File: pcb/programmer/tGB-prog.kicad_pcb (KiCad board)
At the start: 2 copper layers, 25.2 x 31 mm, 40 parts, among them J1 ZX62R-B-5P, J2 PROG_PORT, U1 FT2232D, U2 93LC56BT-I/OT, U3 TPS79901DDCR, Y1 NX8045GB-6MHZ-STD-CSF-3

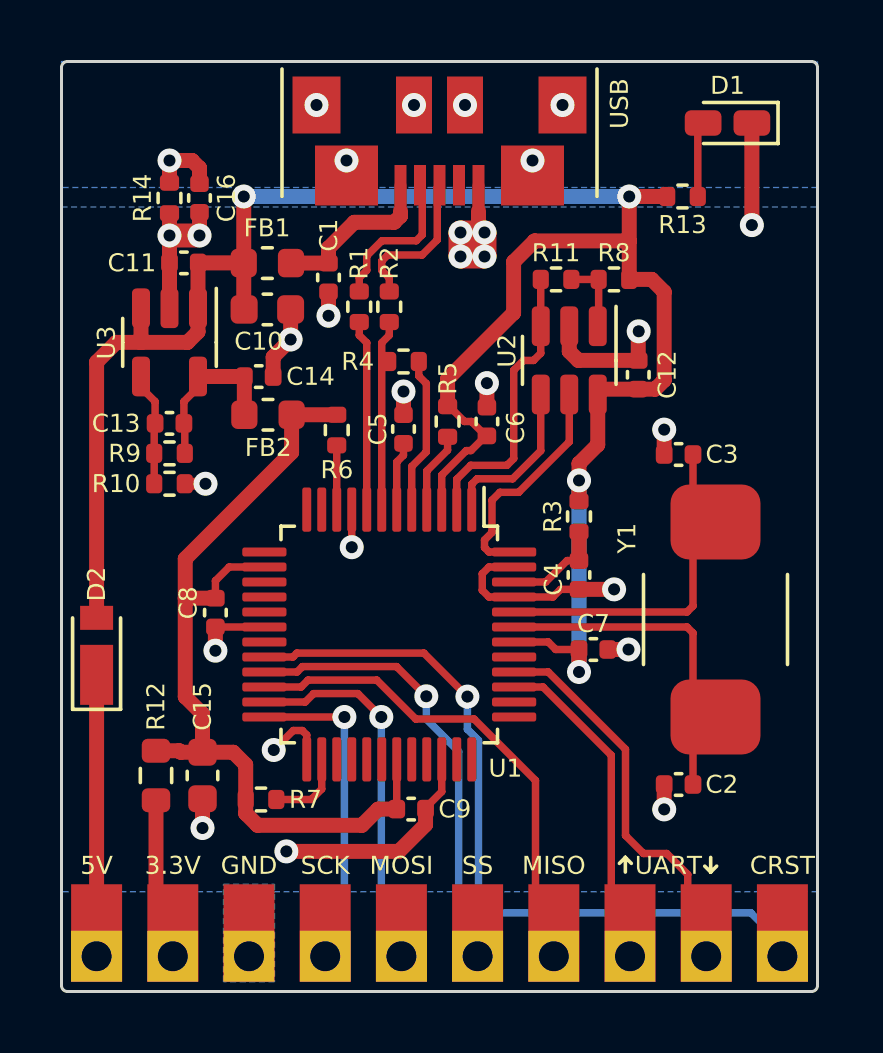
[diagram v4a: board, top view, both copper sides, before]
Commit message: optimize GND and shield zone, fillet USB data tracks
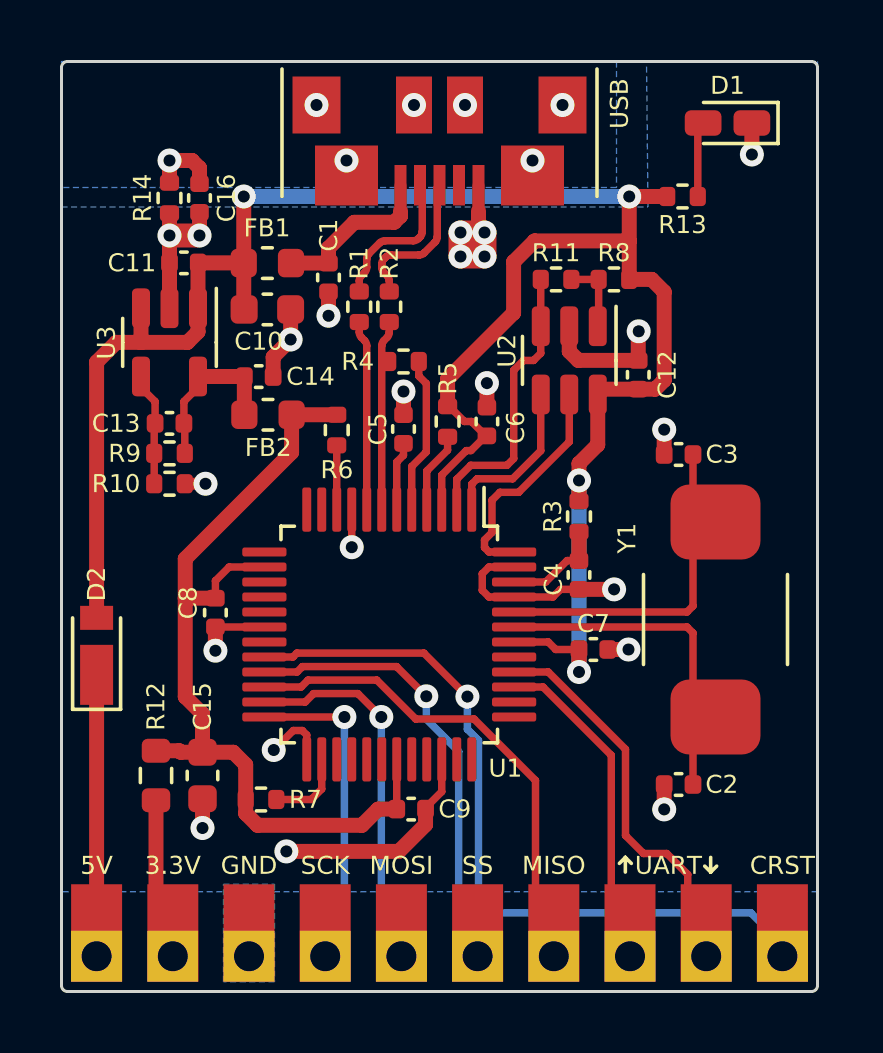
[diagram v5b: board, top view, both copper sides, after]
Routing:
- net GND: track 45.9 -> 43.6 mm
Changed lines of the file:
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@@
   (segment (start 78.9 88.6) (end 78.21 88.6) (width 0.5) (layer "F.Cu") (net 2))
   (segment (start 73.3 74.7) (end 73.3 75.5) (width 0.8) (layer "F.Cu") (net 2))
+  (segment (start 83.0125 71.05) (end 83.0125 72.1) (width 0.5) (layer "F.Cu") (net 2))
   (segment (start 80.09 82.1) (end 80.09 81.27) (width 0.5) (layer "F.Cu") (net 2))
   (segment (start 79.225 78.9625) (end 79.225 78.008052) (width 0.5) (layer "F.Cu") (net 2))
@@
   (segment (start 77.25 86.595) (end 78.42 86.595) (width 0.5) (layer "F.Cu") (net 2))
   (segment (start 67.6375 77.265) (end 67.6375 78.2675) (width 0.5) (layer "F.Cu") (net 2))
-  (segment (start 83.0125 71.05) (end 83.0125 74.4525) (width 0.5) (layer "F.Cu") (net 2))
   (segment (start 68.175 92.2625) (end 68.175 91.45) (width 0.25) (layer "F.Cu") (net 2))
   (segment (start 68.025 91.3) (end 67.725 91.3) (width 0.25) (layer "F.Cu") (net 2))
@@
   (via (at 73.3 75.5) (size 0.8) (drill 0.4) (layers "F.Cu" "B.Cu") (net 2))
   (via (at 67.495 95.33) (size 0.8) (drill 0.4) (layers "F.Cu" "B.Cu") (net 2))
-  (via (at 83.0125 74.4525) (size 0.8) (drill 0.4) (layers "F.Cu" "B.Cu") (net 2))
+  (via (at 83.0125 72.1) (size 0.8) (drill 0.4) (layers "F.Cu" "B.Cu") (net 2))
   (via (at 78.42 86.595) (size 0.8) (drill 0.4) (layers "F.Cu" "B.Cu") (net 2))
   (via (at 79.24 77.993052) (size 0.8) (drill 0.4) (layers "F.Cu" "B.Cu") (net 2))
@@
   (segment (start 62.65 79.865) (end 62.65 79.5) (width 0.25) (layer "F.Cu") (net 8))
   (segment (start 63.12 80.335) (end 62.65 79.865) (width 0.25) (layer "F.Cu") (net 8))
-  (segment (start 70.925 78.125) (end 70.675 78.375) (width 0.25) (layer "F.Cu") (net 9))
+  (segment (start 70.851776 78.198224) (end 70.748223 78.301777) (width 0.25) (layer "F.Cu") (net 9))
   (segment (start 70.675 83.9375) (end 70.675 79) (width 0.25) (layer "F.Cu") (net 9))
-  (segment (start 70.925 77.685) (end 70.925 78.125) (width 0.25) (layer "F.Cu") (net 9))
+  (segment (start 70.925 77.685) (end 70.925 78.021447) (width 0.25) (layer "F.Cu") (net 9))
   (segment (start 70.89 79) (end 70.675 79) (width 0.25) (layer "F.Cu") (net 9))
-  (segment (start 70.675 79) (end 70.675 78.375) (width 0.25) (layer "F.Cu") (net 9))
+  (segment (start 70.675 79) (end 70.675 78.478553) (width 0.25) (layer "F.Cu") (net 9))
+  (arc (start 70.748223 78.301777) (mid 70.69403 78.382883) (end 70.675 78.478553) (width 0.25) (layer "F.Cu") (net 9))
+  (arc (start 70.851776 78.198224) (mid 70.905969 78.117118) (end 70.925 78.021447) (width 0.25) (layer "F.Cu") (net 9))
   (segment (start 61.17 89.475) (end 61.17 98.05) (width 0.5) (layer "F.Cu") (net 10))
   (segment (start 63.15 93.625) (end 63.15 97.49) (width 0.5) (layer "F.Cu") (net 12))
@@
   (segment (start 73.675 83.088604) (end 73.853604 82.91) (width 0.25) (layer "F.Cu") (net 32))
   (segment (start 73.675 83.9375) (end 73.675 83.088604) (width 0.25) (layer "F.Cu") (net 32))
-  (segment (start 70.175 78.375) (end 69.925 78.125) (width 0.25) (layer "F.Cu") (net 35))
-  (segment (start 69.925 78.125) (end 69.925 77.685) (width 0.25) (layer "F.Cu") (net 35))
-  (segment (start 70.175 83.9375) (end 70.175 78.375) (width 0.25) (layer "F.Cu") (net 35))
+  (segment (start 70.101776 78.301776) (end 69.998223 78.198223) (width 0.25) (layer "F.Cu") (net 35))
+  (segment (start 69.925 78.021447) (end 69.925 77.685) (width 0.25) (layer "F.Cu") (net 35))
+  (segment (start 70.175 83.9375) (end 70.175 78.478553) (width 0.25) (layer "F.Cu") (net 35))
+  (arc (start 70.101776 78.301776) (mid 70.155969 78.382882) (end 70.175 78.478553) (width 0.25) (layer "F.Cu") (net 35))
+  (arc (start 69.998223 78.198223) (mid 69.94403 78.117117) (end 69.925 78.021447) (width 0.25) (layer "F.Cu") (net 35))
   (segment (start 75.24 83.36) (end 74.615 83.36) (width 0.25) (layer "F.Cu") (net 46))
   (segment (start 74.1 85.2) (end 74.25 85.35) (width 0.25) (layer "F.Cu") (net 46))
@@
   (segment (start 74.35 84.7) (end 74.1 84.95) (width 0.25) (layer "F.Cu") (net 46))
   (segment (start 74.35 83.625) (end 74.35 84.7) (width 0.25) (layer "F.Cu") (net 46))
-  (segment (start 70.175 75.48) (end 70.175 75.96) (width 0.25) (layer "F.Cu") (net 47))
+  (segment (start 70.175 75.583553) (end 70.175 75.856447) (width 0.25) (layer "F.Cu") (net 47))
   (segment (start 71.95 73.125) (end 72.025 73.2) (width 0.25) (layer "F.Cu") (net 47))
-  (segment (start 70.175 75.96) (end 69.925 76.21) (width 0.25) (layer "F.Cu") (net 47))
-  (segment (start 72.025 73.2) (end 72.025 74.775) (width 0.25) (layer "F.Cu") (net 47))
-  (segment (start 71.825 74.975) (end 70.68 74.975) (width 0.25) (layer "F.Cu") (net 47))
-  (segment (start 70.68 74.975) (end 70.175 75.48) (width 0.25) (layer "F.Cu") (net 47))
-  (segment (start 72.025 74.775) (end 71.825 74.975) (width 0.25) (layer "F.Cu") (net 47))
-  (segment (start 69.925 76.21) (end 69.925 76.65) (width 0.25) (layer "F.Cu") (net 47))
-  (segment (start 72.02 75.45) (end 72.525 74.945) (width 0.25) (layer "F.Cu") (net 48))
-  (segment (start 72.525 74.945) (end 72.525 73.2) (width 0.25) (layer "F.Cu") (net 48))
-  (segment (start 70.675 75.65) (end 70.875 75.45) (width 0.25) (layer "F.Cu") (net 48))
-  (segment (start 70.675 75.96) (end 70.675 75.65) (width 0.25) (layer "F.Cu") (net 48))
-  (segment (start 70.875 75.45) (end 72.02 75.45) (width 0.25) (layer "F.Cu") (net 48))
-  (segment (start 70.925 76.21) (end 70.675 75.96) (width 0.25) (layer "F.Cu") (net 48))
+  (segment (start 70.101776 76.033224) (end 69.998223 76.136777) (width 0.25) (layer "F.Cu") (net 47))
+  (segment (start 72.025 73.2) (end 72.025 74.671447) (width 0.25) (layer "F.Cu") (net 47))
+  (segment (start 71.721447 74.975) (end 70.783553 74.975) (width 0.25) (layer "F.Cu") (net 47))
+  (segment (start 70.606776 75.048224) (end 70.248223 75.406777) (width 0.25) (layer "F.Cu") (net 47))
+  (segment (start 71.951776 74.848224) (end 71.898223 74.901777) (width 0.25) (layer "F.Cu") (net 47))
+  (segment (start 69.925 76.313553) (end 69.925 76.65) (width 0.25) (layer "F.Cu") (net 47))
+  (arc (start 69.998223 76.136777) (mid 69.94403 76.217883) (end 69.925 76.313553) (width 0.25) (layer "F.Cu") (net 47))
+  (arc (start 72.025 74.671447) (mid 72.00597 74.767118) (end 71.951776 74.848224) (width 0.25) (layer "F.Cu") (net 47))
+  (arc (start 70.783553 74.975) (mid 70.687882 74.99403) (end 70.606776 75.048224) (width 0.25) (layer "F.Cu") (net 47))
+  (arc (start 70.175 75.583553) (mid 70.19403 75.487882) (end 70.248223 75.406777) (width 0.25) (layer "F.Cu") (net 47))
+  (arc (start 71.721447 74.975) (mid 71.817118 74.95597) (end 71.898223 74.901777) (width 0.25) (layer "F.Cu") (net 47))
+  (arc (start 70.175 75.856447) (mid 70.15597 75.952118) (end 70.101776 76.033224) (width 0.25) (layer "F.Cu") (net 47))
+  (segment (start 72.093224 75.376776) (end 72.451777 75.018223) (width 0.25) (layer "F.Cu") (net 48))
+  (segment (start 72.525 74.841447) (end 72.525 73.2) (width 0.25) (layer "F.Cu") (net 48))
+  (segment (start 70.748224 75.576776) (end 70.801777 75.523223) (width 0.25) (layer "F.Cu") (net 48))
+  (segment (start 70.675 75.856447) (end 70.675 75.753553) (width 0.25) (layer "F.Cu") (net 48))
+  (segment (start 70.978553 75.45) (end 71.916447 75.45) (width 0.25) (layer "F.Cu") (net 48))
+  (segment (start 70.851776 76.136776) (end 70.748223 76.033223) (width 0.25) (layer "F.Cu") (net 48))
   (segment (start 72.525 73.2) (end 72.6 73.125) (width 0.25) (layer "F.Cu") (net 48))
-  (segment (start 70.925 76.65) (end 70.925 76.21) (width 0.25) (layer "F.Cu") (net 48))
+  (segment (start 70.925 76.65) (end 70.925 76.313553) (width 0.25) (layer "F.Cu") (net 48))
+  (arc (start 72.093224 75.376776) (mid 72.012118 75.430969) (end 71.916447 75.45) (width 0.25) (layer "F.Cu") (net 48))
+  (arc (start 72.451777 75.018223) (mid 72.50597 74.937117) (end 72.525 74.841447) (width 0.25) (layer "F.Cu") (net 48))
+  (arc (start 70.851776 76.136776) (mid 70.905969 76.217882) (end 70.925 76.313553) (width 0.25) (layer "F.Cu") (net 48))
+  (arc (start 70.801777 75.523223) (mid 70.882883 75.46903) (end 70.978553 75.45) (width 0.25) (layer "F.Cu") (net 48))
+  (arc (start 70.748224 75.576776) (mid 70.694031 75.657882) (end 70.675 75.753553) (width 0.25) (layer "F.Cu") (net 48))
+  (arc (start 70.675 75.856447) (mid 70.69403 75.952118) (end 70.748223 76.033223) (width 0.25) (layer "F.Cu") (net 48))
   (segment (start 81.21 73.5) (end 81.21 71.2275) (width 0.25) (layer "F.Cu") (net 49))
   (segment (start 81.21 71.2275) (end 81.3875 71.05) (width 0.25) (layer "F.Cu") (net 49))
@@
         (xy 60 96.675)
         (xy 60 73.85)
-        (xy 85.2 73.85)
+        (xy 79.55 73.85)
+        (xy 79.5 69)
+        (xy 85.2 69)
       )
     )
@@
     (polygon
       (pts
-        (xy 85.2 73.2)
+        (xy 78.5 73.2)
         (xy 60 73.2)
         (xy 60 69)
-        (xy 85.2 69)
+        (xy 78.5 69)
       )
     )

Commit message: set title and revision
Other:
- board text added: "PCB thickness: 0.8mm"
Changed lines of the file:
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@@
   )
   (paper "A4")
+  (title_block
+    (title "tsuraraGB Programmer PCB")
+    (rev "A")
+  )
   (layers
     (0 "F.Cu" signal)
@@
     (effects (font (size 0.6 0.6) (thickness 0.12)))
   )
+  (gr_text "PCB thickness: 0.8mm" (at 87.7 102.5) (layer "Dwgs.User")
+    (effects (font (size 0.6 0.6) (thickness 0.12)) (justify left))
+  )
   (dimension (type aligned) (layer "Dwgs.User")

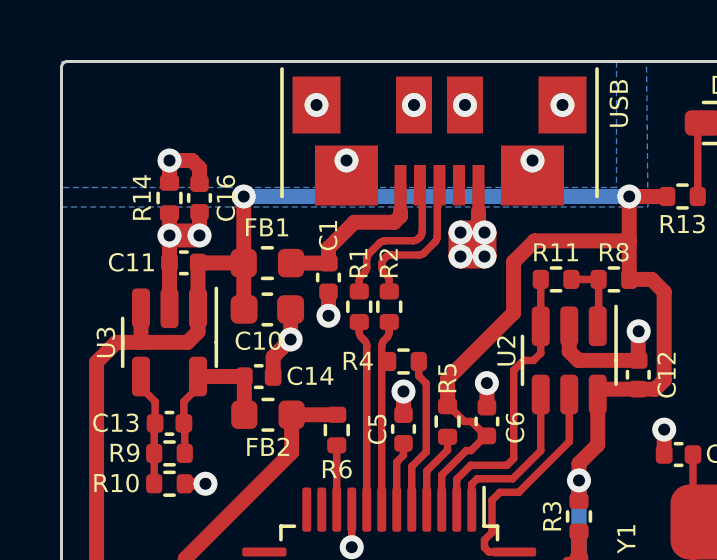
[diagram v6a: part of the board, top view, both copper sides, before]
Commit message: migration from KiCad 6 to 7
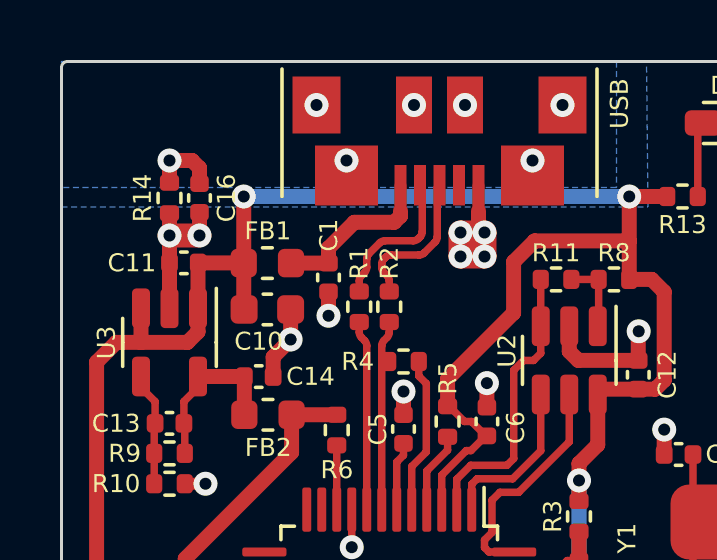
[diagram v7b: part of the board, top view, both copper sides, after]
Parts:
- C15: value DNP -> 4.7μF
- C16: value 10nF -> DNP
- R12: value DNP -> 0Ω
- turned FB1 to 0 degrees
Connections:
- FB1 pad 1: /VBUS -> +5V
- FB1 pad 2: +5V -> /VBUS

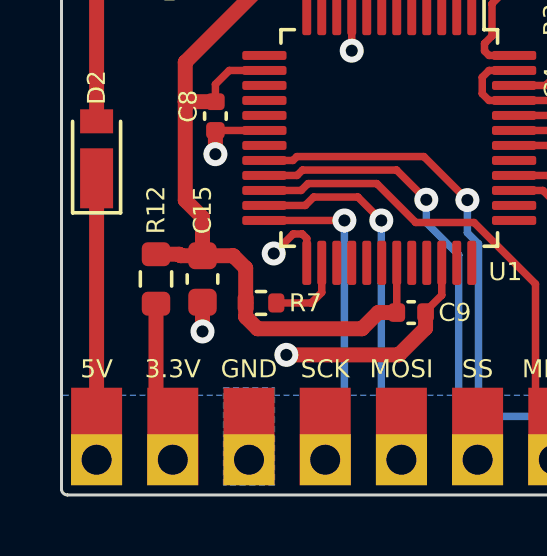
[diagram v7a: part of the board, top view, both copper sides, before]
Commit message: migrate KiCad 7 -> 10
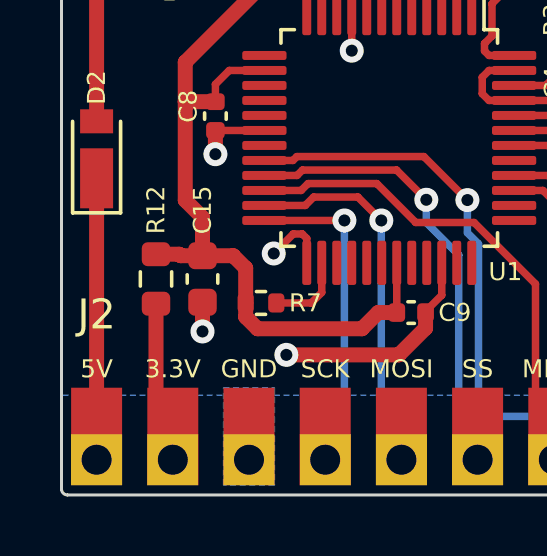
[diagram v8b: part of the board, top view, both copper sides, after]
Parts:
- D1: footprint LED_Addition:LED_0603_1608Metric_Castellated -> ProjectSpecific:LED_0603_1608Metric_Castellated
- J1: footprint ZX62R-B-5P:ZX62R-B-5P -> ProjectSpecific:ZX62R-B-5P
- J2: footprint Pin_Sidemount:PinSocket_1x10_P2.54_Sidemount -> ProjectSpecific:PinSocket_1x10_P2.54_Sidemount
